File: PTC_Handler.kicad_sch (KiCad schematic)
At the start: 10 parts, among them U3 LM397, U4 HCPL-0611

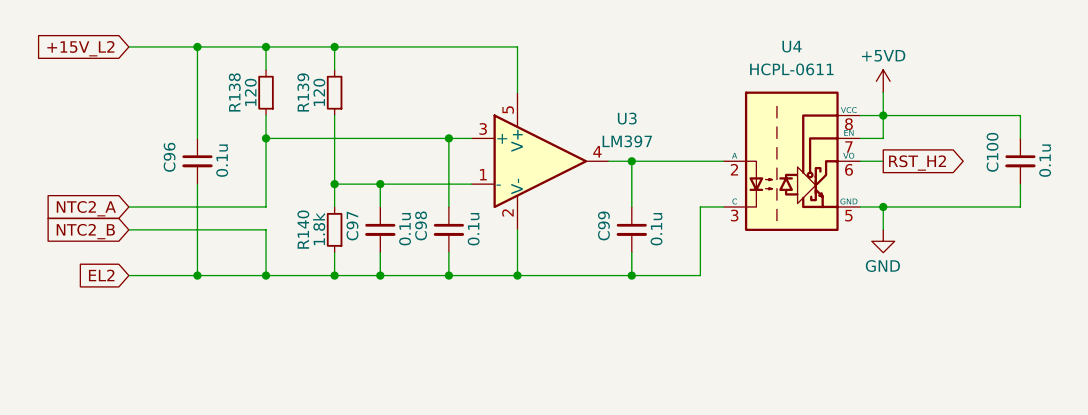
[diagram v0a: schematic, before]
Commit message: Добавил сброс по температуре на все драйвера
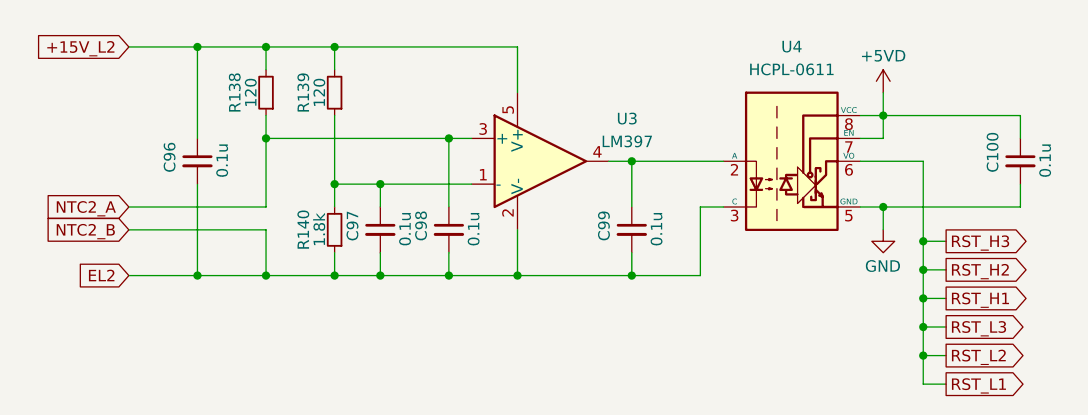
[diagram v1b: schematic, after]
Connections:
- net RST_H2 renamed RST_H1
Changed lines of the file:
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@@
 (kicad_sch (version 20211123) (generator eeschema)
   (paper "A4")
+  (junction (at 197.485 114.935) (diameter 0) (color 0 0 0 0)
+  )
   (junction (at 137.16 99.06) (diameter 0) (color 0 0 0 0)
   )
@@
   (junction (at 124.46 109.22) (diameter 0) (color 0 0 0 0)
   )
+  (junction (at 197.485 105.41) (diameter 0) (color 0 0 0 0)
+  )
   (junction (at 152.4 109.22) (diameter 0) (color 0 0 0 0)
   )
+  (junction (at 197.485 118.11) (diameter 0) (color 0 0 0 0)
+  )
   (junction (at 124.46 83.82) (diameter 0) (color 0 0 0 0)
   )
@@
   (junction (at 116.84 109.22) (diameter 0) (color 0 0 0 0)
   )
+  (junction (at 197.485 108.585) (diameter 0) (color 0 0 0 0)
+  )
   (junction (at 132.08 83.82) (diameter 0) (color 0 0 0 0)
   )
+  (junction (at 197.485 111.76) (diameter 0) (color 0 0 0 0)
+  )
   (junction (at 165.1 96.52) (diameter 0) (color 0 0 0 0)
   )
@@
     (stroke (width 0) (type default) (color 0 0 0 0))
   )
+  (wire (pts (xy 197.485 118.11) (xy 197.485 121.285))
+    (stroke (width 0) (type default) (color 0 0 0 0))
+  )
   (wire (pts (xy 190.5 101.6) (xy 193.04 101.6))
     (stroke (width 0) (type default) (color 0 0 0 0))
@@
     (stroke (width 0) (type default) (color 0 0 0 0))
   )
-  (wire (pts (xy 190.5 96.52) (xy 193.04 96.52))
-    (stroke (width 0) (type default) (color 0 0 0 0))
-  )
   (wire (pts (xy 116.84 109.22) (xy 124.46 109.22))
     (stroke (width 0) (type default) (color 0 0 0 0))
@@
     (stroke (width 0) (type default) (color 0 0 0 0))
   )
+  (wire (pts (xy 200.025 111.76) (xy 197.485 111.76))
+    (stroke (width 0) (type default) (color 0 0 0 0))
+  )
   (wire (pts (xy 152.4 83.82) (xy 152.4 88.9))
     (stroke (width 0) (type default) (color 0 0 0 0))
   )
+  (wire (pts (xy 197.485 96.52) (xy 197.485 105.41))
+    (stroke (width 0) (type default) (color 0 0 0 0))
+  )
   (wire (pts (xy 144.78 109.22) (xy 152.4 109.22))
     (stroke (width 0) (type default) (color 0 0 0 0))
@@
     (stroke (width 0) (type default) (color 0 0 0 0))
   )
+  (wire (pts (xy 197.485 121.285) (xy 200.025 121.285))
+    (stroke (width 0) (type default) (color 0 0 0 0))
+  )
   (wire (pts (xy 124.46 93.98) (xy 124.46 101.6))
     (stroke (width 0) (type default) (color 0 0 0 0))
@@
     (stroke (width 0) (type default) (color 0 0 0 0))
   )
+  (wire (pts (xy 197.485 105.41) (xy 200.025 105.41))
+    (stroke (width 0) (type default) (color 0 0 0 0))
+  )
   (wire (pts (xy 172.72 109.22) (xy 165.1 109.22))
     (stroke (width 0) (type default) (color 0 0 0 0))
@@
     (stroke (width 0) (type default) (color 0 0 0 0))
   )
+  (wire (pts (xy 197.485 111.76) (xy 197.485 114.935))
+    (stroke (width 0) (type default) (color 0 0 0 0))
+  )
   (wire (pts (xy 137.16 109.22) (xy 132.08 109.22))
     (stroke (width 0) (type default) (color 0 0 0 0))
   )
+  (wire (pts (xy 197.485 111.76) (xy 197.485 108.585))
+    (stroke (width 0) (type default) (color 0 0 0 0))
+  )
+  (wire (pts (xy 197.485 118.11) (xy 200.025 118.11))
+    (stroke (width 0) (type default) (color 0 0 0 0))
+  )
   (wire (pts (xy 165.1 96.52) (xy 175.26 96.52))
     (stroke (width 0) (type default) (color 0 0 0 0))
@@
     (stroke (width 0) (type default) (color 0 0 0 0))
   )
+  (wire (pts (xy 197.485 108.585) (xy 197.485 105.41))
+    (stroke (width 0) (type default) (color 0 0 0 0))
+  )
   (wire (pts (xy 193.04 91.44) (xy 193.04 88.9))
     (stroke (width 0) (type default) (color 0 0 0 0))
   )
+  (wire (pts (xy 197.485 114.935) (xy 197.485 118.11))
+    (stroke (width 0) (type default) (color 0 0 0 0))
+  )
   (wire (pts (xy 116.84 99.06) (xy 116.84 109.22))
     (stroke (width 0) (type default) (color 0 0 0 0))
@@
     (stroke (width 0) (type default) (color 0 0 0 0))
   )
+  (wire (pts (xy 190.5 96.52) (xy 197.485 96.52))
+    (stroke (width 0) (type default) (color 0 0 0 0))
+  )
   (wire (pts (xy 132.08 86.36) (xy 132.08 83.82))
     (stroke (width 0) (type default) (color 0 0 0 0))
@@
     (stroke (width 0) (type default) (color 0 0 0 0))
   )
+  (wire (pts (xy 200.025 108.585) (xy 197.485 108.585))
+    (stroke (width 0) (type default) (color 0 0 0 0))
+  )
+  (wire (pts (xy 197.485 114.935) (xy 200.025 114.935))
+    (stroke (width 0) (type default) (color 0 0 0 0))
+  )
   (wire (pts (xy 144.78 106.68) (xy 144.78 109.22))
     (stroke (width 0) (type default) (color 0 0 0 0))
@@
     (stroke (width 0) (type default) (color 0 0 0 0))
   )
-  (global_label "RST_H2" (shape output) (at 193.04 96.52 0) (fields_autoplaced)
-    (effects (font (size 1.27 1.27)) (justify left))
-    (property "Intersheet References" "${INTERSHEET_REFS}" (id 0) (at 202.4079 96.4406 0)
+  (global_label "RST_H3" (shape output) (at 200.025 105.41 0) (fields_autoplaced)
+    (effects (font (size 1.27 1.27)) (justify left))
+    (property "Intersheet References" "${INTERSHEET_REFS}" (id 0) (at 209.3929 105.3306 0)
+      (effects (font (size 1.27 1.27)) (justify left) hide)
+    )
+  )
+  (global_label "RST_L3" (shape output) (at 200.025 114.935 0) (fields_autoplaced)
+    (effects (font (size 1.27 1.27)) (justify left))
+    (property "Intersheet References" "${INTERSHEET_REFS}" (id 0) (at 209.0905 114.8556 0)
       (effects (font (size 1.27 1.27)) (justify left) hide)
     )
@@
     )
   )
+  (global_label "RST_L1" (shape output) (at 200.025 121.285 0) (fields_autoplaced)
+    (effects (font (size 1.27 1.27)) (justify left))
+    (property "Intersheet References" "${INTERSHEET_REFS}" (id 0) (at 209.0905 121.2056 0)
+      (effects (font (size 1.27 1.27)) (justify left) hide)
+    )
+  )
+  (global_label "RST_H2" (shape output) (at 200.025 108.585 0) (fields_autoplaced)
+    (effects (font (size 1.27 1.27)) (justify left))
+    (property "Intersheet References" "${INTERSHEET_REFS}" (id 0) (at 209.3929 108.5056 0)
+      (effects (font (size 1.27 1.27)) (justify left) hide)
+    )
+  )
+  (global_label "RST_H1" (shape output) (at 200.025 111.76 0) (fields_autoplaced)
+    (effects (font (size 1.27 1.27)) (justify left))
+    (property "Intersheet References" "${INTERSHEET_REFS}" (id 0) (at 209.3929 111.6806 0)
+      (effects (font (size 1.27 1.27)) (justify left) hide)
+    )
+  )
+  (global_label "RST_L2" (shape output) (at 200.025 118.11 0) (fields_autoplaced)
+    (effects (font (size 1.27 1.27)) (justify left))
+    (property "Intersheet References" "${INTERSHEET_REFS}" (id 0) (at 209.0905 118.0306 0)
+      (effects (font (size 1.27 1.27)) (justify left) hide)
+    )
+  )

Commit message: Исправмл логику защиты по температуре
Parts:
- removed C99: 0.1u, Capacitor_SMD:C_0805_2012Metric_Pad1.18x1.45mm_HandSolder, symbol Device:C_Small
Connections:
- net +15V_L2: now also U4.2 (A)
- net EL2: no longer U4.3 (C)
- net at U3.4: now also U4.3 (C); no longer U4.2 (A)
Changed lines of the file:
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@@
   (junction (at 116.84 83.82) (diameter 0) (color 0 0 0 0)
   )
-  (junction (at 165.1 109.22) (diameter 0) (color 0 0 0 0)
-  )
   (junction (at 193.04 101.6) (diameter 0) (color 0 0 0 0)
   )
   (junction (at 132.08 99.06) (diameter 0) (color 0 0 0 0)
   )
+  (junction (at 152.4 83.82) (diameter 0) (color 0 0 0 0)
+  )
   (junction (at 124.46 109.22) (diameter 0) (color 0 0 0 0)
   )
   (junction (at 197.485 105.41) (diameter 0) (color 0 0 0 0)
   )
-  (junction (at 152.4 109.22) (diameter 0) (color 0 0 0 0)
-  )
   (junction (at 197.485 118.11) (diameter 0) (color 0 0 0 0)
   )
@@
   (junction (at 197.485 111.76) (diameter 0) (color 0 0 0 0)
   )
-  (junction (at 165.1 96.52) (diameter 0) (color 0 0 0 0)
-  )
   (junction (at 144.78 109.22) (diameter 0) (color 0 0 0 0)
   )
@@
     (stroke (width 0) (type default) (color 0 0 0 0))
   )
+  (wire (pts (xy 152.4 83.82) (xy 175.26 83.82))
+    (stroke (width 0) (type default) (color 0 0 0 0))
+  )
   (wire (pts (xy 200.025 111.76) (xy 197.485 111.76))
     (stroke (width 0) (type default) (color 0 0 0 0))
@@
     (stroke (width 0) (type default) (color 0 0 0 0))
   )
-  (wire (pts (xy 175.26 101.6) (xy 172.72 101.6))
+  (wire (pts (xy 165.735 101.6) (xy 175.26 101.6))
     (stroke (width 0) (type default) (color 0 0 0 0))
   )
@@
     (stroke (width 0) (type default) (color 0 0 0 0))
   )
-  (wire (pts (xy 162.56 96.52) (xy 165.1 96.52))
-    (stroke (width 0) (type default) (color 0 0 0 0))
-  )
   (wire (pts (xy 132.08 106.68) (xy 132.08 109.22))
     (stroke (width 0) (type default) (color 0 0 0 0))
   )
-  (wire (pts (xy 172.72 101.6) (xy 172.72 109.22))
-    (stroke (width 0) (type default) (color 0 0 0 0))
-  )
   (wire (pts (xy 109.22 109.22) (xy 116.84 109.22))
     (stroke (width 0) (type default) (color 0 0 0 0))
@@
     (stroke (width 0) (type default) (color 0 0 0 0))
   )
+  (wire (pts (xy 175.26 96.52) (xy 175.26 83.82))
+    (stroke (width 0) (type default) (color 0 0 0 0))
+  )
   (wire (pts (xy 197.485 121.285) (xy 200.025 121.285))
     (stroke (width 0) (type default) (color 0 0 0 0))
@@
     (stroke (width 0) (type default) (color 0 0 0 0))
   )
-  (wire (pts (xy 165.1 106.68) (xy 165.1 109.22))
-    (stroke (width 0) (type default) (color 0 0 0 0))
-  )
   (wire (pts (xy 144.78 109.22) (xy 137.16 109.22))
     (stroke (width 0) (type default) (color 0 0 0 0))
@@
     (stroke (width 0) (type default) (color 0 0 0 0))
   )
-  (wire (pts (xy 172.72 109.22) (xy 165.1 109.22))
-    (stroke (width 0) (type default) (color 0 0 0 0))
-  )
   (wire (pts (xy 190.5 91.44) (xy 193.04 91.44))
     (stroke (width 0) (type default) (color 0 0 0 0))
@@
     (stroke (width 0) (type default) (color 0 0 0 0))
   )
-  (wire (pts (xy 165.1 96.52) (xy 175.26 96.52))
-    (stroke (width 0) (type default) (color 0 0 0 0))
-  )
-  (wire (pts (xy 165.1 96.52) (xy 165.1 101.6))
-    (stroke (width 0) (type default) (color 0 0 0 0))
-  )
   (wire (pts (xy 109.22 104.14) (xy 124.46 104.14))
     (stroke (width 0) (type default) (color 0 0 0 0))
@@
     (stroke (width 0) (type default) (color 0 0 0 0))
   )
+  (wire (pts (xy 165.735 96.52) (xy 165.735 101.6))
+    (stroke (width 0) (type default) (color 0 0 0 0))
+  )
   (wire (pts (xy 132.08 83.82) (xy 152.4 83.82))
     (stroke (width 0) (type default) (color 0 0 0 0))
@@
     (stroke (width 0) (type default) (color 0 0 0 0))
   )
-  (wire (pts (xy 165.1 109.22) (xy 152.4 109.22))
+  (wire (pts (xy 162.56 96.52) (xy 165.735 96.52))
     (stroke (width 0) (type default) (color 0 0 0 0))
   )
@@
   )
   (symbol (lib_id "Comparator:LM397") (at 154.94 96.52 0) (unit 1)
-    (in_bom yes) (on_board yes) (fields_autoplaced)
-    (property "Reference" "U3" (id 0) (at 164.592 91.821 0))
-    (property "Value" "LM397" (id 1) (at 164.592 94.361 0))
+    (in_bom yes) (on_board yes)
+    (property "Reference" "U3" (id 0) (at 156.845 90.17 0))
+    (property "Value" "LM397" (id 1) (at 156.845 92.075 0))
     (property "Footprint" "Package_TO_SOT_SMD:SOT-23-5" (id 2) (at 156.21 111.76 0)
       (effects (font (size 1.27 1.27)) hide)
@@
       (effects (font (size 1.27 1.27)) hide)
     )
-    (pin "1")
-    (pin "2")
-  )
-  (symbol (lib_id "Device:C_Small") (at 165.1 104.14 0) (unit 1)
-    (in_bom yes) (on_board yes)
-    (property "Reference" "C99" (id 0) (at 162.052 105.41 90)
-      (effects (font (size 1.27 1.27)) (justify left))
-    )
-    (property "Value" "0.1u" (id 1) (at 167.894 102.108 90)
-      (effects (font (size 1.27 1.27)) (justify right))
-    )
-    (property "Footprint" "Capacitor_SMD:C_0805_2012Metric_Pad1.18x1.45mm_HandSolder" (id 2) (at 165.1 104.14 0)
-      (effects (font (size 1.27 1.27)) hide)
-    )
-    (property "Datasheet" "~" (id 3) (at 165.1 104.14 0)
-      (effects (font (size 1.27 1.27)) hide)
-    )

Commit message: Добавил подтяжку к HCPL
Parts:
- added R?: 300, Resistor_SMD:R_0805_2012Metric_Pad1.20x1.40mm_HandSolder, symbol Device:R_Small
- R138, R139: value 120 -> 1k
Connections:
- net +15V_L2: now also R?.2; no longer U4.2 (A)
- new net: R?.1, U4.2 (A)
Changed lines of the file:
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@@
     (stroke (width 0) (type default) (color 0 0 0 0))
   )
-  (wire (pts (xy 152.4 83.82) (xy 175.26 83.82))
+  (wire (pts (xy 152.4 83.82) (xy 161.925 83.82))
     (stroke (width 0) (type default) (color 0 0 0 0))
   )
@@
   )
   (wire (pts (xy 197.485 114.935) (xy 197.485 118.11))
+    (stroke (width 0) (type default) (color 0 0 0 0))
+  )
+  (wire (pts (xy 167.005 83.82) (xy 175.26 83.82))
     (stroke (width 0) (type default) (color 0 0 0 0))
   )
@@
   (symbol (lib_id "Device:C_Small") (at 116.84 96.52 0) (unit 1)
     (in_bom yes) (on_board yes)
-    (property "Reference" "C96" (id 0) (at 113.792 97.79 90)
-      (effects (font (size 1.27 1.27)) (justify left))
-    )
-    (property "Value" "0.1u" (id 1) (at 119.634 94.488 90)
+    (property "Reference" "C96" (id 0) (at 112.395 94.615 0)
+      (effects (font (size 1.27 1.27)) (justify left))
+    )
+    (property "Value" "0.1u" (id 1) (at 116.205 98.425 0)
       (effects (font (size 1.27 1.27)) (justify right))
     )
@@
   (symbol (lib_id "Device:R_Small") (at 124.46 88.9 180) (unit 1)
     (in_bom yes) (on_board yes)
-    (property "Reference" "R138" (id 0) (at 121.031 88.9 90))
-    (property "Value" "120" (id 1) (at 122.809 88.9 90))
+    (property "Reference" "R138" (id 0) (at 121.285 86.36 0))
+    (property "Value" "1k" (id 1) (at 121.92 88.9 0))
     (property "Footprint" "Resistor_SMD:R_0805_2012Metric_Pad1.20x1.40mm_HandSolder" (id 2) (at 124.46 88.9 0)
       (effects (font (size 1.27 1.27)) hide)
@@
   (symbol (lib_id "Device:R_Small") (at 132.08 104.14 180) (unit 1)
     (in_bom yes) (on_board yes)
-    (property "Reference" "R140" (id 0) (at 128.651 104.14 90))
-    (property "Value" "1.8k" (id 1) (at 130.429 104.14 90))
+    (property "Reference" "R140" (id 0) (at 128.27 102.87 0))
+    (property "Value" "1.8k" (id 1) (at 128.905 105.41 0))
     (property "Footprint" "Resistor_SMD:R_0805_2012Metric_Pad1.20x1.40mm_HandSolder" (id 2) (at 132.08 104.14 0)
       (effects (font (size 1.27 1.27)) hide)
@@
   (symbol (lib_id "Device:C_Small") (at 137.16 104.14 0) (unit 1)
     (in_bom yes) (on_board yes)
-    (property "Reference" "C97" (id 0) (at 134.112 105.41 90)
-      (effects (font (size 1.27 1.27)) (justify left))
-    )
-    (property "Value" "0.1u" (id 1) (at 139.954 102.108 90)
+    (property "Reference" "C97" (id 0) (at 133.35 102.235 0)
+      (effects (font (size 1.27 1.27)) (justify left))
+    )
+    (property "Value" "0.1u" (id 1) (at 137.16 106.045 0)
       (effects (font (size 1.27 1.27)) (justify right))
     )
@@
   (symbol (lib_id "Device:C_Small") (at 144.78 104.14 0) (unit 1)
     (in_bom yes) (on_board yes)
-    (property "Reference" "C98" (id 0) (at 141.732 105.41 90)
-      (effects (font (size 1.27 1.27)) (justify left))
-    )
-    (property "Value" "0.1u" (id 1) (at 147.574 102.108 90)
+    (property "Reference" "C98" (id 0) (at 140.97 102.235 0)
+      (effects (font (size 1.27 1.27)) (justify left))
+    )
+    (property "Value" "0.1u" (id 1) (at 144.78 106.045 0)
       (effects (font (size 1.27 1.27)) (justify right))
     )
@@
   (symbol (lib_id "Device:R_Small") (at 132.08 88.9 180) (unit 1)
     (in_bom yes) (on_board yes)
-    (property "Reference" "R139" (id 0) (at 128.651 88.9 90))
-    (property "Value" "120" (id 1) (at 130.429 88.9 90))
+    (property "Reference" "R139" (id 0) (at 128.905 86.36 0))
+    (property "Value" "1k" (id 1) (at 129.54 88.9 0))
     (property "Footprint" "Resistor_SMD:R_0805_2012Metric_Pad1.20x1.40mm_HandSolder" (id 2) (at 132.08 88.9 0)
       (effects (font (size 1.27 1.27)) hide)
@@
     (pin "1")
   )
+  (symbol (lib_id "Device:R_Small") (at 164.465 83.82 270) (unit 1)
+    (in_bom yes) (on_board yes)
+    (property "Reference" "R?" (id 0) (at 164.465 81.915 90))
+    (property "Value" "300" (id 1) (at 164.465 85.471 90))
+    (property "Footprint" "Resistor_SMD:R_0805_2012Metric_Pad1.20x1.40mm_HandSolder" (id 2) (at 164.465 83.82 0)
+      (effects (font (size 1.27 1.27)) hide)
+    )
+    (property "Datasheet" "~" (id 3) (at 164.465 83.82 0)
+      (effects (font (size 1.27 1.27)) hide)
+    )
+    (pin "1")
+    (pin "2")
+  )
   (symbol (lib_id "Device:C_Small") (at 208.28 96.52 0) (unit 1)
     (in_bom yes) (on_board yes)
-    (property "Reference" "C100" (id 0) (at 205.232 97.79 90)
-      (effects (font (size 1.27 1.27)) (justify left))
-    )
-    (property "Value" "0.1u" (id 1) (at 211.074 94.488 90)
+    (property "Reference" "C100" (id 0) (at 202.565 94.615 0)
+      (effects (font (size 1.27 1.27)) (justify left))
+    )
+    (property "Value" "0.1u" (id 1) (at 207.645 98.425 0)
       (effects (font (size 1.27 1.27)) (justify right))
     )
